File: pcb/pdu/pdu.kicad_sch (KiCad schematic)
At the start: 6 parts, among them J1 CONN_PCIE_PWR_8PIN, J2 MOLEX_0039291087, J3 CONN_01X04, J4 CONN_01X04, J5 CONN_IBC_MGMT_DEVICE, J6 CONN_IBC_MGMT_HOST

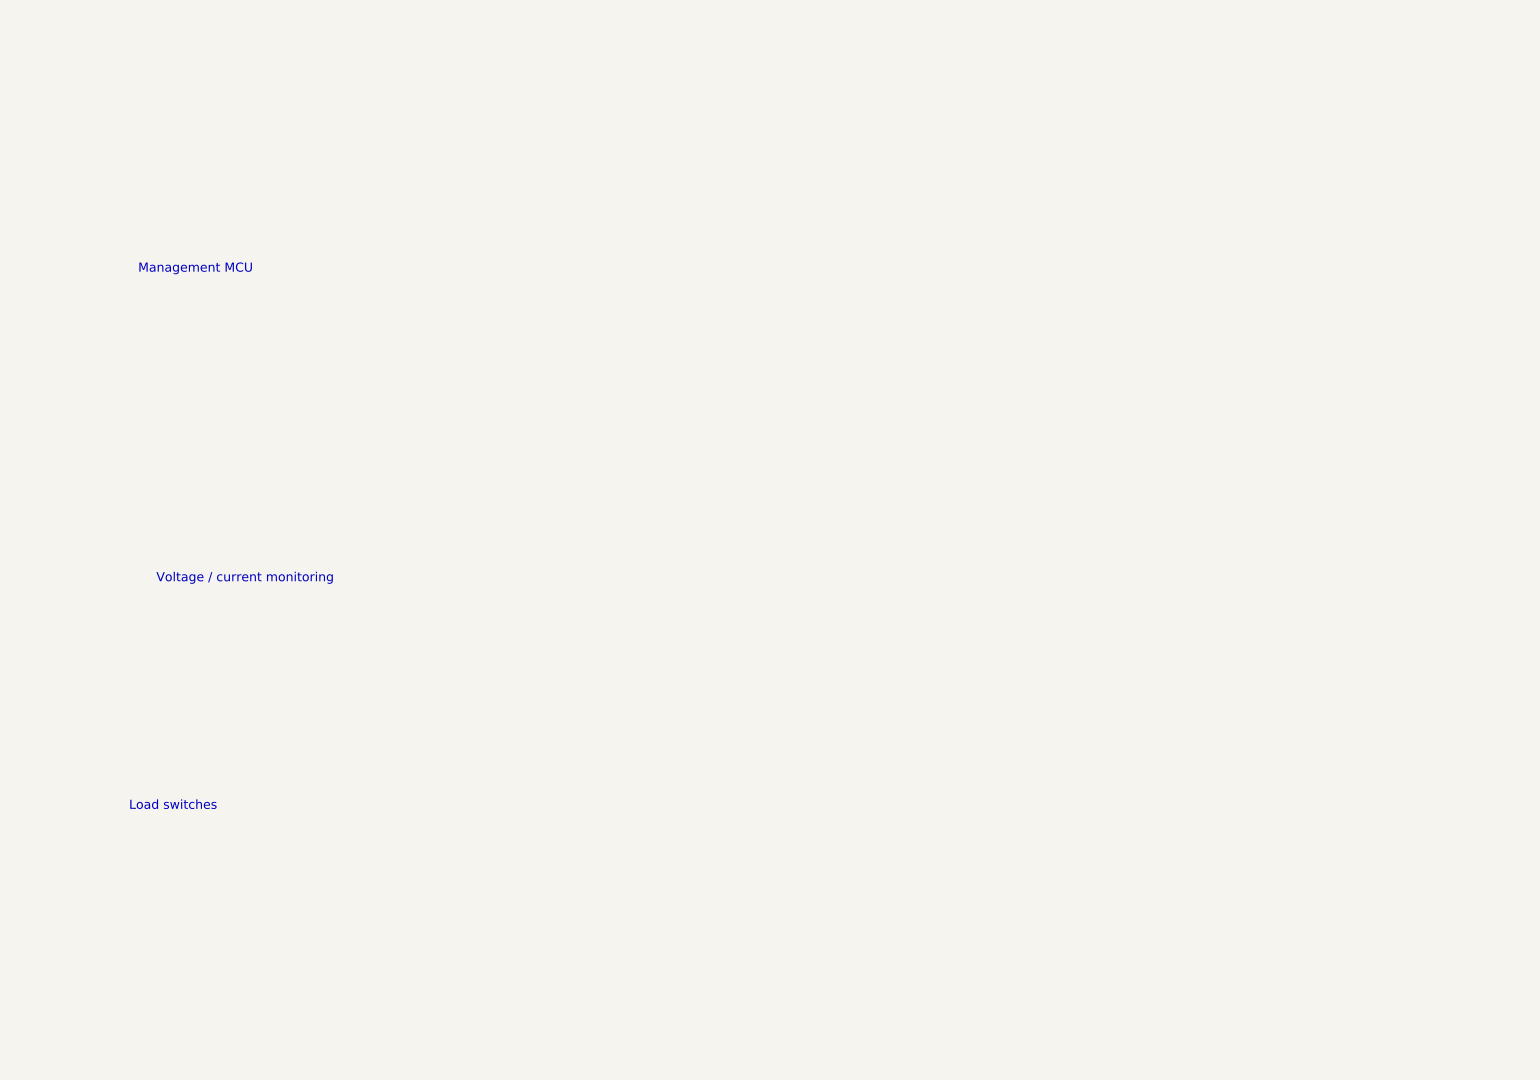
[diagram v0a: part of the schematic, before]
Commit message: Continued power routing on right PHY
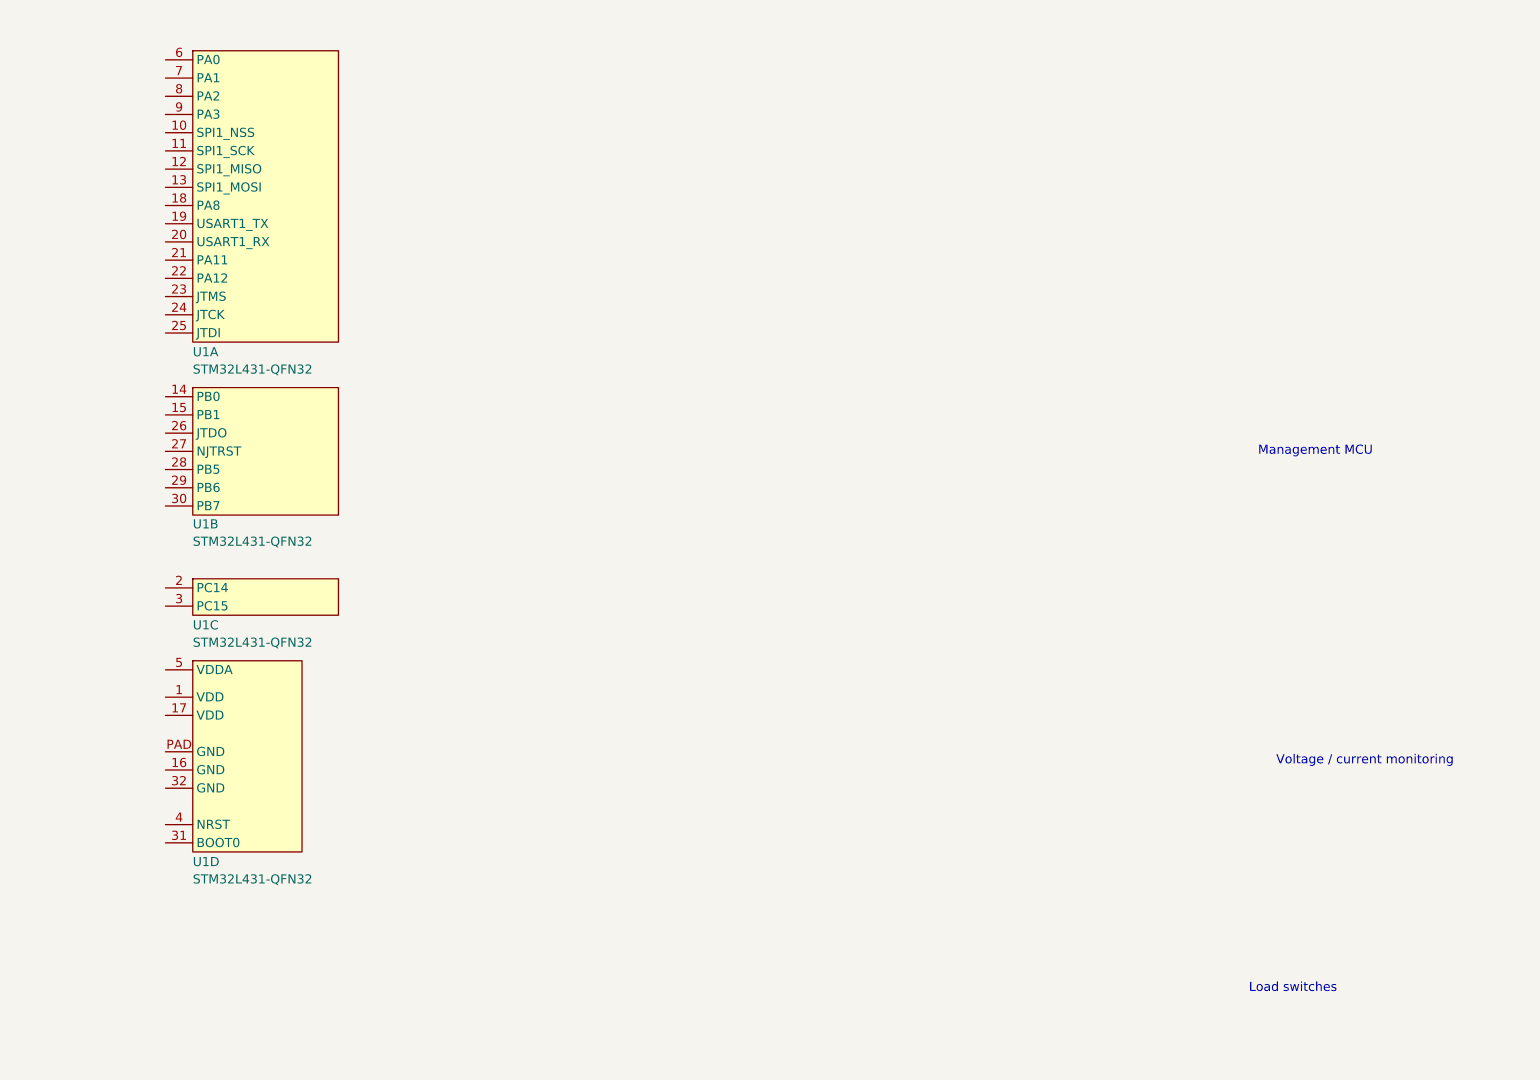
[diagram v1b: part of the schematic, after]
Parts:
- added U1: STM32L431-QFN32, symbol st-azonenberg:STM32L431-QFN32

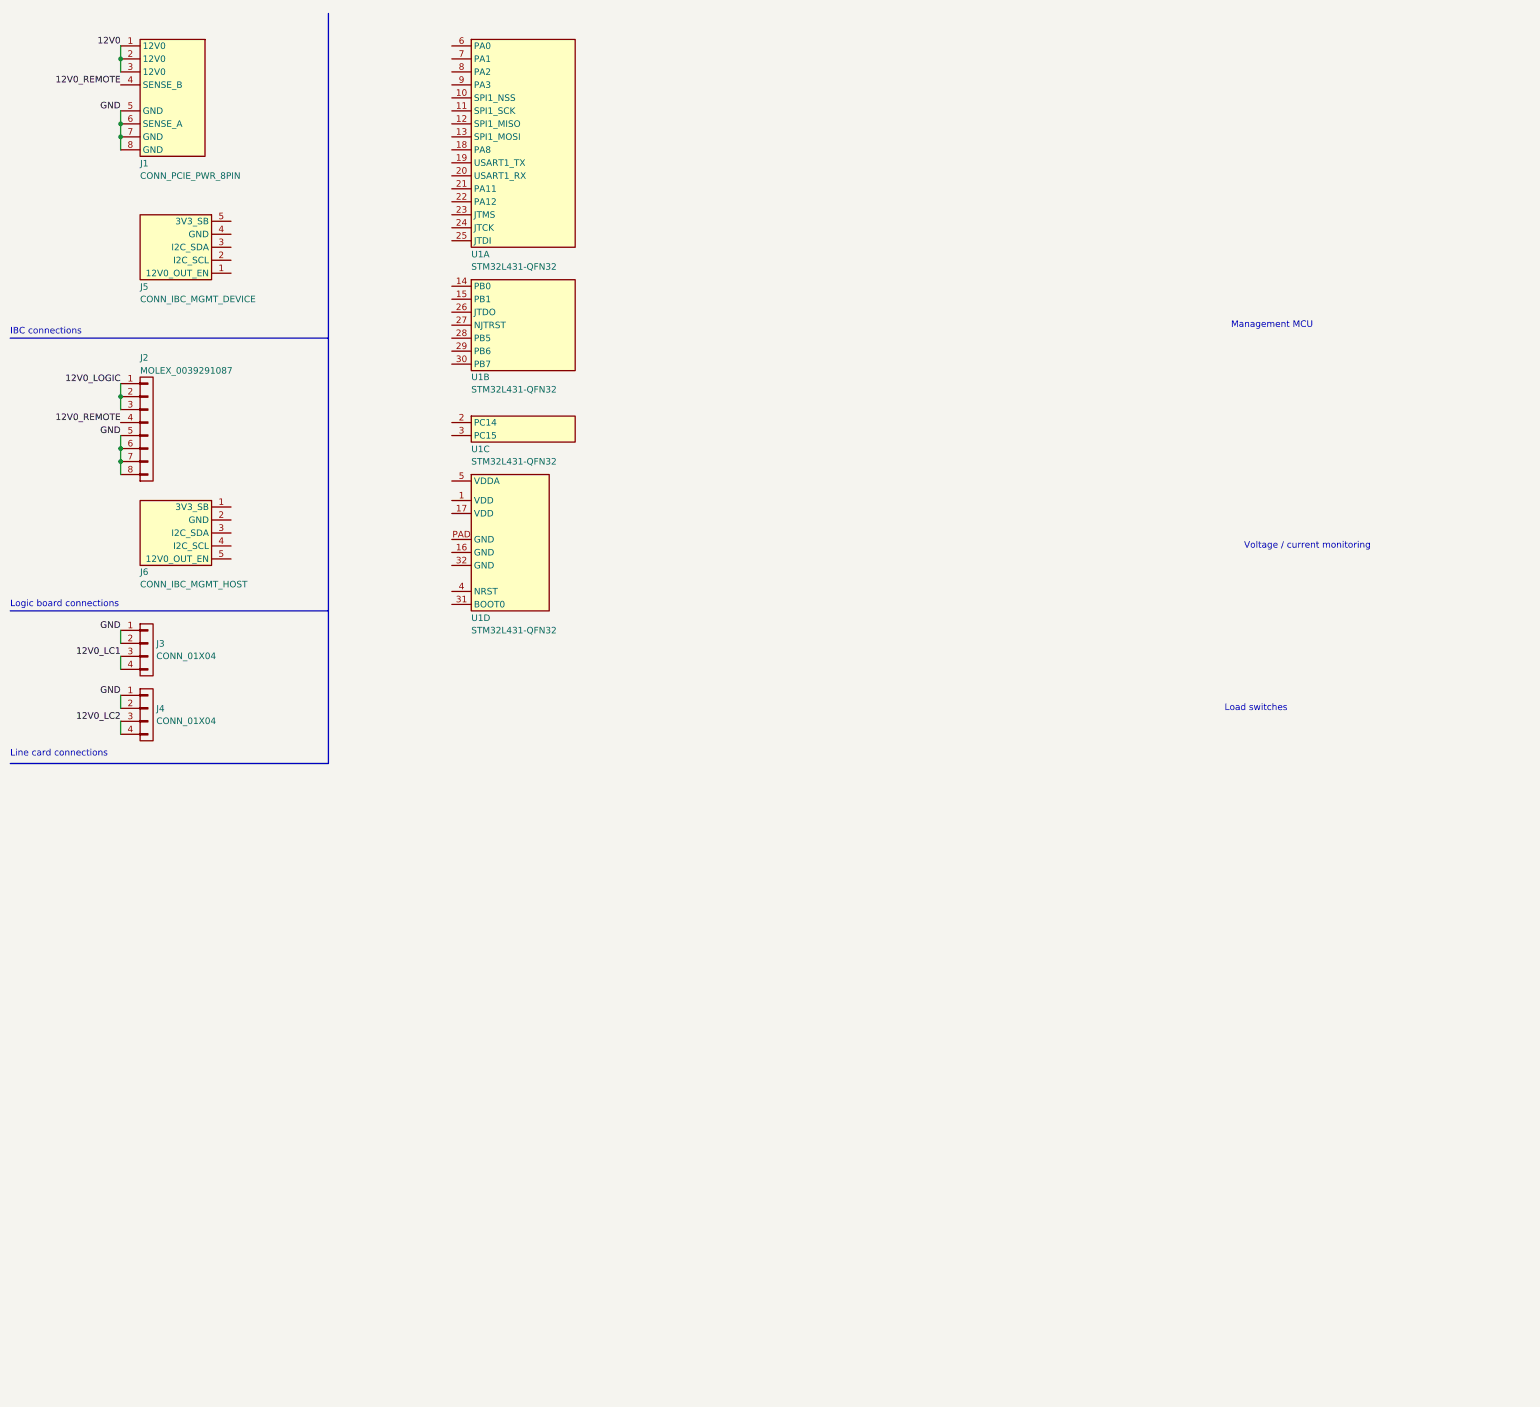
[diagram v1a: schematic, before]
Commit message: Initial version of PDU board is done, ready for review
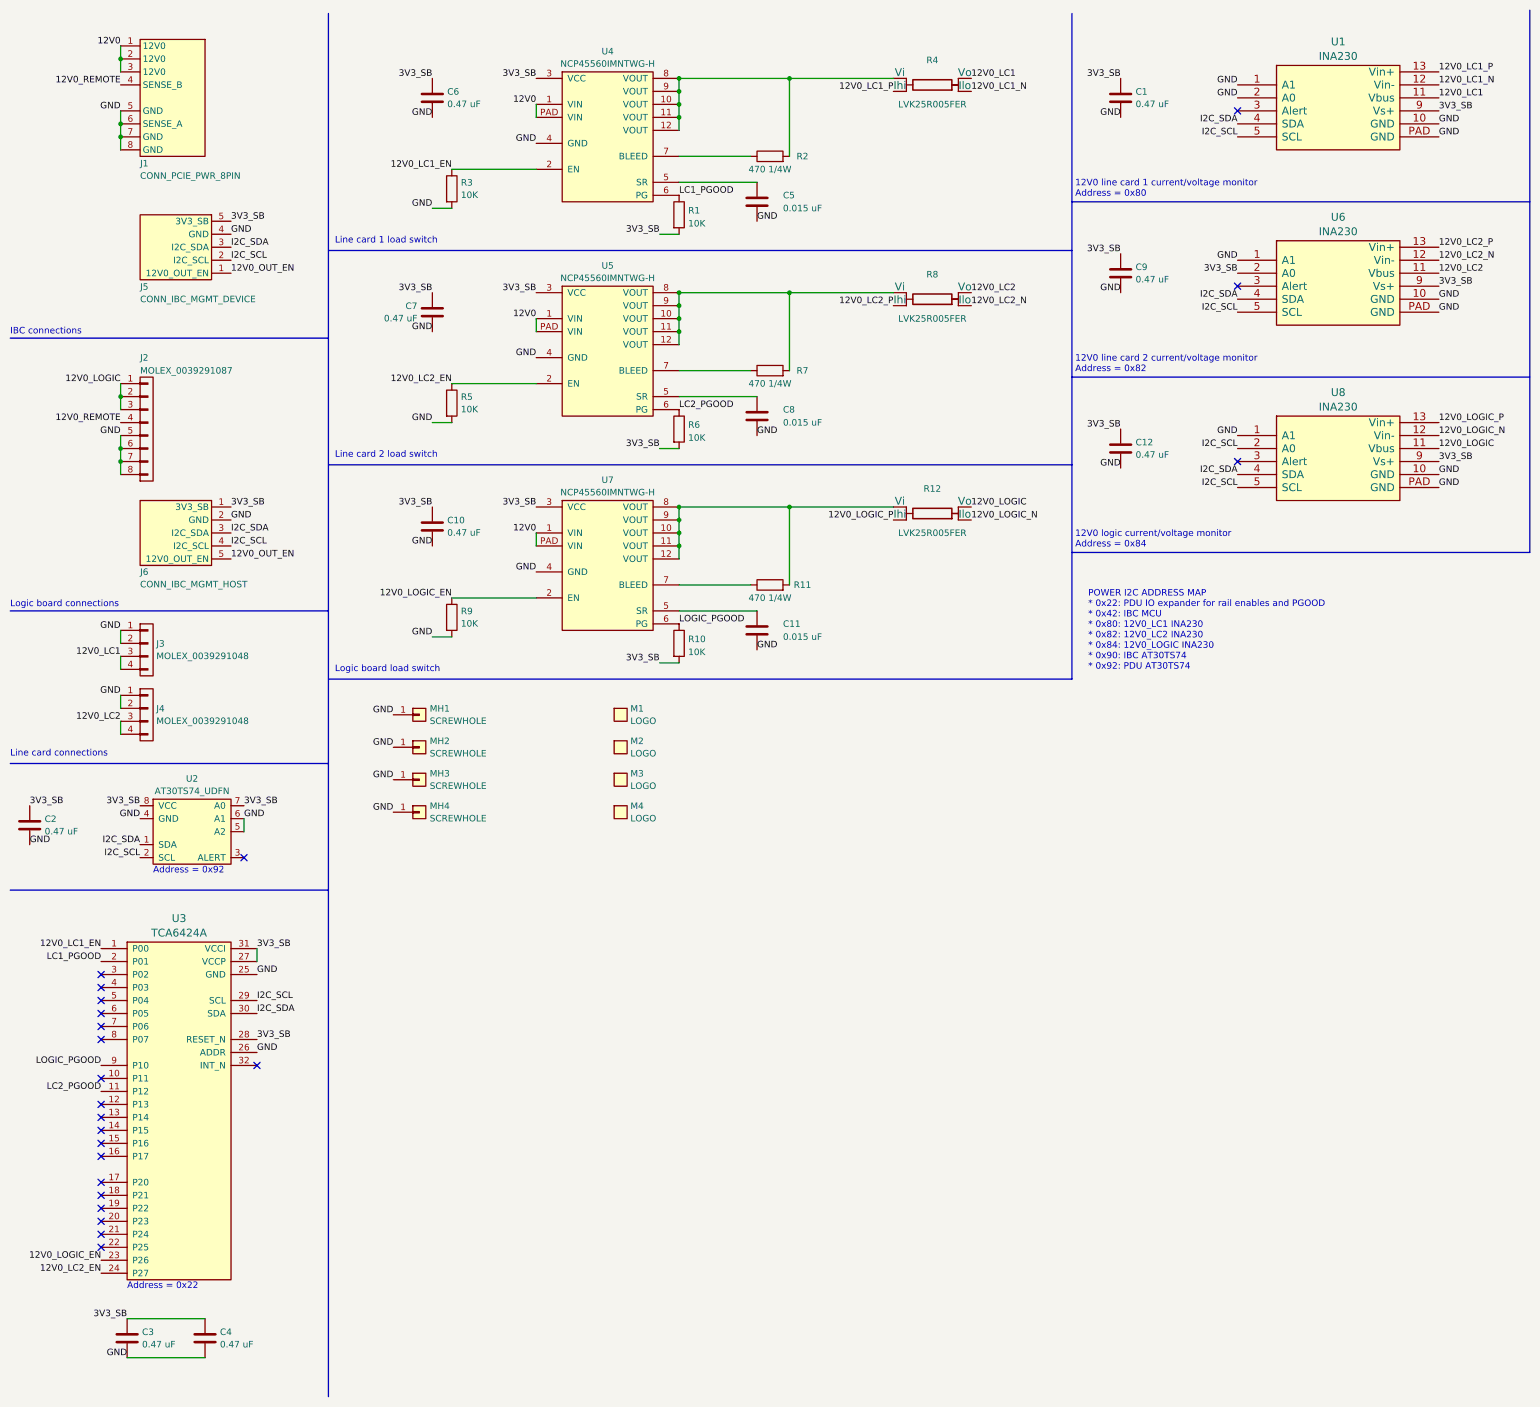
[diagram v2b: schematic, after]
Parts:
- removed U1: STM32L431-QFN32, symbol st-azonenberg:STM32L431-QFN32
- added C1, C10, C12, C2, C3, C4, C6, C7, C9: 0.47 uF, azonenberg_pcb:EIA_0402_CAP_NOSILK, symbol device:C
- added C11, C5, C8: 0.015 uF, azonenberg_pcb:EIA_0603_CAP_NOSILK, symbol device:C
- added M1: LOGO, azonenberg_pcb:LONGTHING-1200DPI, symbol special-azonenberg:MECHANICAL
- added M2: LOGO, w_logo:Logo_silk_WEEE_3.4x5mm, symbol special-azonenberg:MECHANICAL
- added M3: LOGO, w_logo:Logo_silk_ROHS_5x2.8mm, symbol special-azonenberg:MECHANICAL
- added M4: LOGO, w_logo:Logo_silk_OSHW_6x6mm, symbol special-azonenberg:MECHANICAL
- added MH1, MH2, MH3, MH4: SCREWHOLE, azonenberg_pcb:MECHANICAL_CLEARANCEHOLE_4_40, symbol Connector:Conn_01x01
- added R1, R10, R3, R5, R6, R9: 10K, azonenberg_pcb:EIA_0402_RES_NOSILK, symbol device:R
- added R11, R2, R7: 470 1/4W, azonenberg_pcb:EIA_0603_RES_NOSILK, symbol device:R
- added R12, R4, R8: LVK25R005FER, azonenberg_pcb:OHMITE_LVK25, symbol passive-azonenberg:R-4TERM
- added U1, U6, U8: INA230, azonenberg_pcb:QFN_16_0.5MM_3x3MM, symbol special-azonenberg:INA230
- added U2: AT30TS74_UDFN, azonenberg_pcb:DFN_8_0.5MM_2x3MM_TALL, symbol special-azonenberg:AT30TS74_UDFN
- added U3: TCA6424A, azonenberg_pcb:QFN_32_0.5MM_5x5MM, symbol special-azonenberg:TCA6424A
- added U4, U5, U7: NCP45560IMNTWG-H, azonenberg_pcb:DFN_12_0.5MM_3x3MM, symbol power-azonenberg:NCP45560
- J1: footprint (none) -> azonenberg_pcb:CONN_MOLEX_MINIFITJR_8POS_0039291087
- J3, J4: value CONN_01X04 -> MOLEX_0039291048; footprint (none) -> azonenberg_pcb:CONN_MOLEX_MINIFITJR_4POS_0039291048
- J5, J6: footprint (none) -> azonenberg_pcb:CONN_MOLEX_PICOBLADE_5POS_0532610571
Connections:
- net 12V0: now also U4.1 (VIN), U4.PAD (VIN), U5.1 (VIN), U5.PAD (VIN), U7.1 (VIN), U7.PAD (VIN)
- net 12V0_LC1: now also R4.2 (Vo), U1.11 (Vbus)
- net 12V0_LC2: now also R8.2 (Vo), U6.11 (Vbus)
- net 12V0_LOGIC: now also R12.2 (Vo), U8.11 (Vbus)
- net GND: now also J5.4 (GND), J6.2 (GND), C1.2, C10.2, C11.2, C12.2, C2.2, C3.2, C4.2, C5.2, C6.2, C7.2, C8.2, C9.2, MH1.1 (Pin_1), MH2.1 (Pin_1), MH3.1 (Pin_1), MH4.1 (Pin_1), R3.2, R5.2, R9.2, U1.1 (A1), U1.10 (GND), U1.2 (A0), U1.PAD (GND), U2.4 (GND), U2.5 (A2), U2.6 (A1), U3.25 (GND), U3.26 (ADDR), U4.4 (GND), U5.4 (GND), U6.1 (A1), U6.10 (GND), U6.PAD (GND), U7.4 (GND), U8.1 (A1), U8.10 (GND), U8.PAD (GND)
- net 12V0_OUT_EN: now reaches J5.1 (12V0_OUT_EN)
- net 12V0_OUT_EN: now also J6.5 (12V0_OUT_EN)
- net I2C_SCL: now reaches J5.2 (I2C_SCL)
- net I2C_SCL: now also J6.4 (I2C_SCL), U1.5 (SCL), U2.2 (SCL), U3.29 (SCL), U6.5 (SCL), U8.2 (A0), U8.5 (SCL)
- net I2C_SDA: now reaches J5.3 (I2C_SDA)
- net I2C_SDA: now also J6.3 (I2C_SDA), U1.4 (SDA), U2.1 (SDA), U3.30 (SDA), U6.4 (SDA), U8.4 (SDA)
- net 3V3_SB: now reaches J5.5 (3V3_SB)
- net 3V3_SB: now also J6.1 (3V3_SB), C1.1, C10.1, C12.1, C2.1, C3.1, C4.1, C6.1, C7.1, C9.1, R1.2, R10.2, R6.2, U1.9 (Vs+), U2.7 (A0), U2.8 (VCC), U3.27 (VCCP), U3.28 (RESET_N), U3.31 (VCCI), U4.3 (VCC), U5.3 (VCC), U6.2 (A0), U6.9 (Vs+), U7.3 (VCC), U8.9 (Vs+)
- new net: R11.2, R12.4 (Vi), U7.10 (VOUT), U7.11 (VOUT), U7.12 (VOUT), U7.8 (VOUT), U7.9 (VOUT)
- new net: R2.2, R4.4 (Vi), U4.10 (VOUT), U4.11 (VOUT), U4.12 (VOUT), U4.8 (VOUT), U4.9 (VOUT)
- new net: R7.2, R8.4 (Vi), U5.10 (VOUT), U5.11 (VOUT), U5.12 (VOUT), U5.8 (VOUT), U5.9 (VOUT)
- new net: R2.1, U4.7 (BLEED)
- new net: C8.1, U5.5 (SR)
- new net: R7.1, U5.7 (BLEED)
- new net: C11.1, U7.5 (SR)
- new net: R11.1, U7.7 (BLEED)
- new net: C5.1, U4.5 (SR)
- new net 12V0_LC1_EN: R3.1, U3.1 (P00), U4.2 (EN)
- new net 12V0_LC1_N: R4.1 (Ilo), U1.12 (Vin-)
- new net 12V0_LC1_P: R4.3 (Ihi), U1.13 (Vin+)
- new net 12V0_LC2_EN: R5.1, U3.24 (P27), U5.2 (EN)
- new net 12V0_LC2_N: R8.1 (Ilo), U6.12 (Vin-)
- new net 12V0_LC2_P: R8.3 (Ihi), U6.13 (Vin+)
- new net 12V0_LOGIC_EN: R9.1, U3.23 (P26), U7.2 (EN)
- new net 12V0_LOGIC_N: R12.1 (Ilo), U8.12 (Vin-)
- new net 12V0_LOGIC_P: R12.3 (Ihi), U8.13 (Vin+)
- new net LC1_PGOOD: R1.1, U3.2 (P01), U4.6 (PG)
- new net LC2_PGOOD: R6.1, U3.11 (P12), U5.6 (PG)
- new net LOGIC_PGOOD: R10.1, U3.9 (P10), U7.6 (PG)
- no-connect marks 0 -> 23
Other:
- note added: "12V0 line card 1 current/voltage monitor Address = 0x80"
- note added: "12V0 line card 2 current/voltage monitor Address = 0x82"
- note added: "12V0 logic current/voltage monitor Address = 0x84"
- note added: "Address = 0x22"
- note added: "Address = 0x92"
- note added: "Line card 1 load switch"
- note added: "Line card 2 load switch"
- note added: "Logic board load switch"
- note added: "POWER I2C ADDRESS MAP * 0x22: PDU IO expander for rail enables and PGOOD * 0x42: IBC MCU * 0x80: 12V0_LC1 INA230 * 0x82: 12V0_LC2 INA230 * 0x84: 12V0_LOGIC INA230 * 0x90: IBC AT30TS74 * 0x92: PDU AT30TS74"
- note removed: "Load switches"
- note removed: "Management MCU"
- note removed: "Voltage / current monitoring"
